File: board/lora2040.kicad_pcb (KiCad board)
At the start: 2 copper layers, 19 parts, among them U1 RP2040, U2 MR20H40, U3 RFM9xBreakout, Y1 ABM8-272-T3

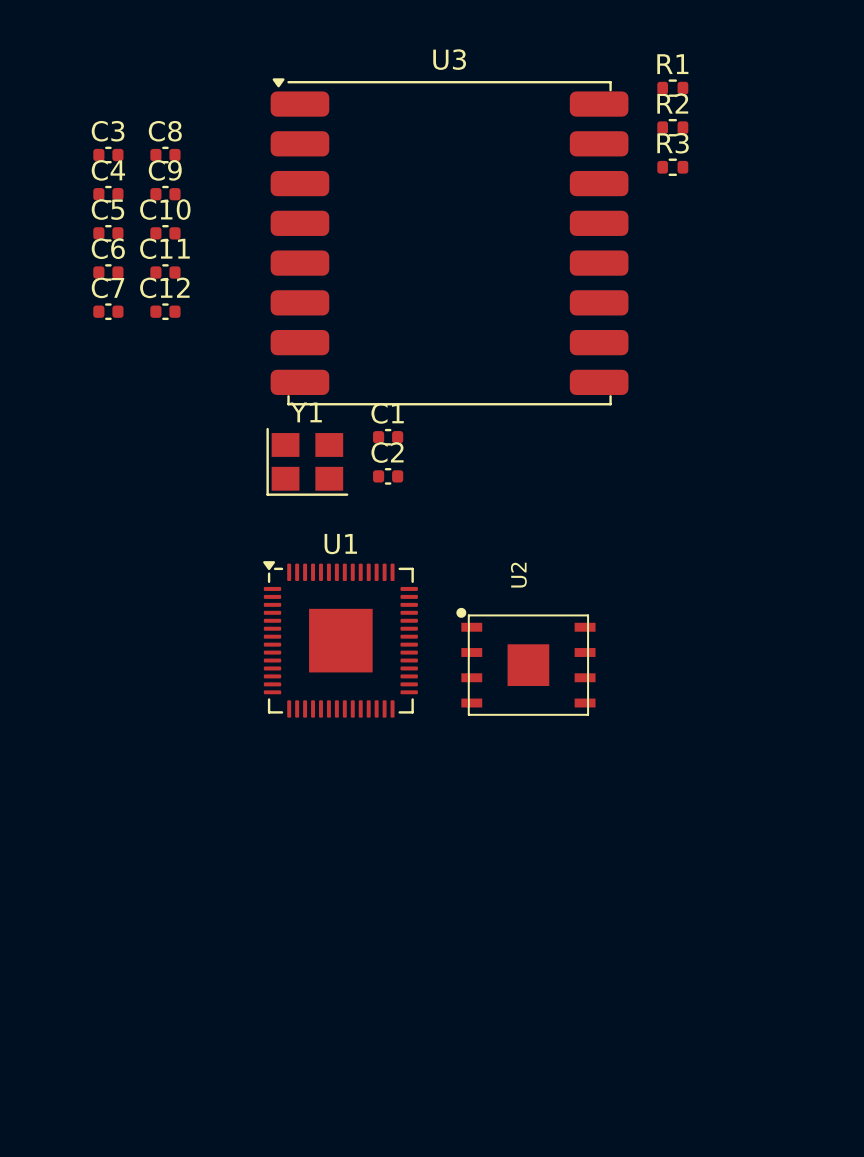
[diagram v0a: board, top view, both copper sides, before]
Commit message: added in sx1262 ref design
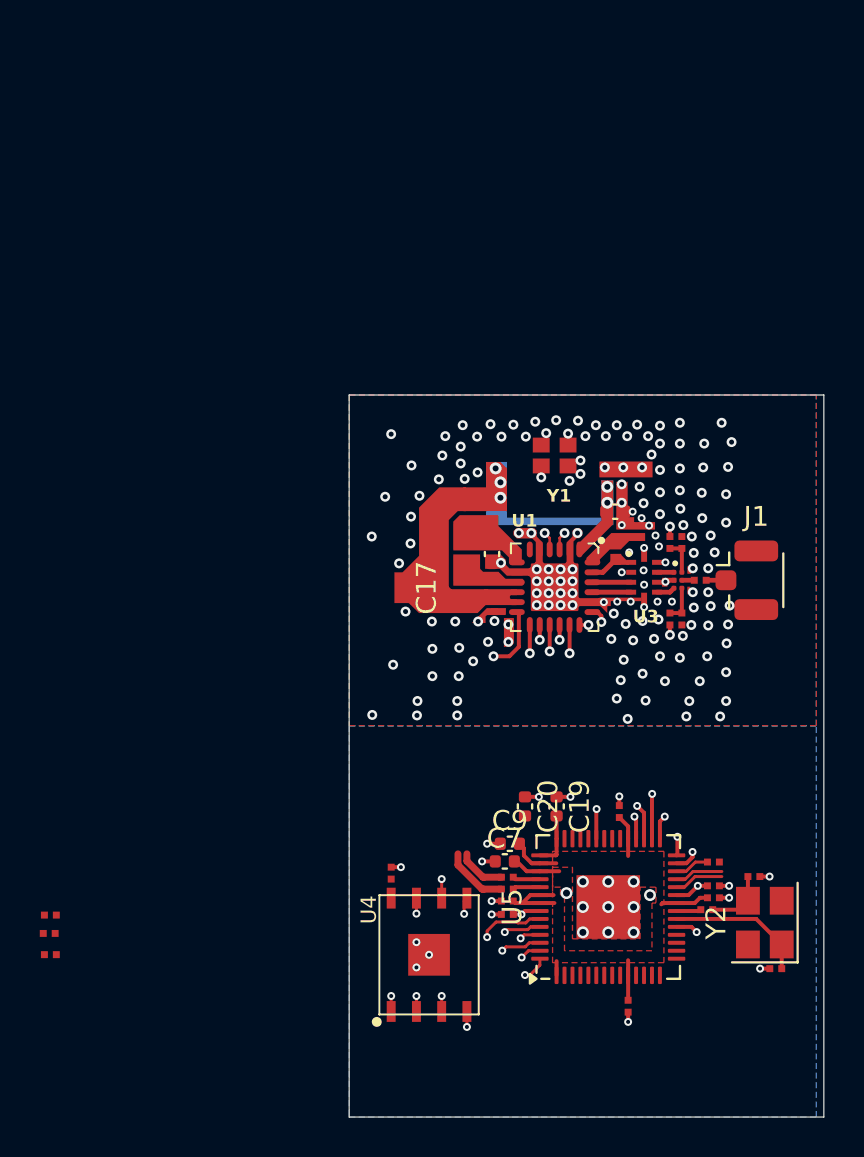
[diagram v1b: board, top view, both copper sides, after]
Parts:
- added C13: 0.1uF, custom-footprints:sx126x_C_0201, F.Cu at (151.0, 105.2)
- added C14: 1nF, custom-footprints:sx126x_C_0201, F.Cu at (149.4, 87.3)
- added C15: 1nF, custom-footprints:sx126x_C_0201, F.Cu at (149.4, 91.2)
- added C16: 0.1uF, Capacitor_SMD:C_0402_1005Metric, F.Cu at (146.1, 85.8)
- added C17: 470nF, Capacitor_SMD:C_0402_1005Metric, F.Cu at (139.9, 87.9)
- added C18: 0.1uF, custom-footprints:sx126x_C_0201, F.Cu at (140.0, 90.5)
- added C19: 0.1uF, Capacitor_SMD:C_0402_1005Metric, F.Cu at (143.1, 100.6)
- added C20: 0.1uF, Capacitor_SMD:C_0402_1005Metric, F.Cu at (141.6, 100.6)
- added C21: 0.1uF, custom-footprints:sx126x_C_0201, F.Cu at (134.8, 103.9)
- added J1: u.FL, Connector_Coaxial:U.FL_Hirose_U.FL-R-SMT-1_Vertical, F.Cu at (152.7, 89.2)
- added L1: 47nF, custom-footprints:sx126x_L_0402, F.Cu at (146.1, 87.8)
- added L7: 15uH, custom-footprints:sx126x_L_0805, F.Cu at (138.6, 87.8)
- added R4: 100, custom-footprints:sx126x_R_0201, F.Cu at (148.8, 87.3)
- added R5: 0, custom-footprints:sx126x_R_0201, F.Cu at (117.7, 108.0)
- added R6: 27, custom-footprints:sx126x_R_0201, F.Cu at (140.7, 104.7)
- added R7: 27, custom-footprints:sx126x_R_0201, F.Cu at (140.7, 104.1)
- added R8: 1K, custom-footprints:sx126x_R_0201, F.Cu at (150.7, 105.8)
- added R9: 10K, custom-footprints:sx126x_R_0201, F.Cu at (151.0, 103.4)
- added U4: MR20H40 or AS3004204, custom-footprints:SON127P600X500X90-9N, F.Cu at (136.7, 108.0)
- added U5: RP2040, Package_DFN_QFN:QFN-56-1EP_7x7mm_P0.4mm_EP3.2x3.2mm, F.Cu at (145.7, 105.6)
- added Y2: ABM8-272-T3, Crystal:Crystal_SMD_3225-4Pin_3.2x2.5mm, F.Cu at (153.6, 106.4)
- C1: value 15pF -> 47nF; footprint Capacitor_SMD:C_0402_1005Metric -> custom-footprints:sx126x_C_0201
- C10, C11, C12, C5: footprint Capacitor_SMD:C_0402_1005Metric -> custom-footprints:sx126x_C_0201
- C2: value 15pF -> 47pF; footprint Capacitor_SMD:C_0402_1005Metric -> custom-footprints:sx126x_C_0201
- C3: value 1uF -> 15pF; footprint Capacitor_SMD:C_0402_1005Metric -> custom-footprints:sx126x_C_0201
- C4: value 0.1uF -> 15pF; footprint Capacitor_SMD:C_0402_1005Metric -> custom-footprints:sx126x_C_0201
- C6: value 1uF -> 0.1uF; footprint Capacitor_SMD:C_0402_1005Metric -> custom-footprints:sx126x_C_0201
- C7, C9: value 0.1uF -> 1uF
- C8: value 0.1uF -> 39pF; footprint Capacitor_SMD:C_0402_1005Metric -> custom-footprints:sx126x_C_0201
- R1: value 27 -> 10K; footprint Resistor_SMD:R_0402_1005Metric -> custom-footprints:sx126x_R_0201
- R2: footprint Resistor_SMD:R_0402_1005Metric -> custom-footprints:sx126x_R_0201
- R3: value 27 -> 100; footprint Resistor_SMD:R_0402_1005Metric -> custom-footprints:sx126x_R_0201
- U1: value RP2040 -> SX1262IMLTRT; footprint Package_DFN_QFN:QFN-56-1EP_7x7mm_P0.4mm_EP3.2x3.2mm -> custom-footprints:VQFN24_4X4MM_SX126x
- U2: value MR20H40 -> BGS12WN6E6327; footprint custom-footprints:SON127P600X500X90-9N -> Package_LGA:Infineon_PG-TSNP-6-10_0.7x1.1mm_0.7x1.1mm_P0.4mm
- U3: value RFM9xBreakout -> 0900FM15K0039; footprint RF_Module:HOPERF_RFM9XW_SMD -> custom-footprints:0900FM15K0039
- Y1: value ABM8-272-T3 -> EXS00A-CS06465; footprint Crystal:Crystal_SMD_3225-4Pin_3.2x2.5mm -> custom-footprints:sx126x_Xtal
- moved C3 52.9 mm to (154.2, 108.7)
- moved R1 52.8 mm to (117.6, 107.0)
- moved R2 50.5 mm to (117.7, 106.0)
- moved C4 47.3 mm to (153.1, 104.1), turned to 180 degrees
- moved C10 45.3 mm to (146.7, 110.6), turned to 90 degrees
- moved C5 44.8 mm to (151.0, 104.6), turned to 180 degrees
- moved C6 38.0 mm to (140.7, 106.0)
- moved C9 37.0 mm to (140.8, 102.5)
- moved C11 36.0 mm to (140.7, 105.3)
- moved C8 34.4 mm to (150.4, 89.2), turned to 180 degrees
- moved C7 34.1 mm to (140.5, 103.3)
- moved C12 34.0 mm to (146.3, 100.8), turned to -90 degrees
- moved R3 22.7 mm to (148.8, 91.2), turned to -90 degrees
- moved U3 19.4 mm to (147.5, 89.1), turned to -90 degrees
- moved C2 13.1 mm to (147.4, 86.8), turned to -90 degrees
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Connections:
- C1 pad 2: /XIN -> Net-(U1-VR_PA)
- C10 pad 1: Net-(C10-Pad1) -> GND
- C11 pad 1: Net-(C10-Pad1) -> GND
- C12 pad 1: Net-(C10-Pad1) -> GND
- C2 pad 2: Net-(C2-Pad2) -> Net-(U1-VR_PA)
- C3 pad 2: +1V1 -> /XIN
- C4 pad 2: +1V1 -> Net-(C4-Pad2)
- C6 pad 2: +3V3 -> +1V1
- C7 pad 1: Net-(C10-Pad1) -> GND
- C7 pad 2: +3V3 -> +1V1
- C8 pad 1: Net-(C10-Pad1) -> Net-(J1-In)
- C8 pad 2: +3V3 -> Net-(U2-RFIN)
- C9 pad 1: Net-(C10-Pad1) -> GND
- R1 pad 1: /USB_D+ -> /QSPI_SS
- R1 pad 2: Net-(U1-USB_DP) -> +3V3
- R2 pad 1: Net-(C2-Pad2) -> Net-(R2-Pad1)
- R2 pad 2: /XOUT -> /QSPI_SS
- R3 pad 1: /USB_D- -> Net-(U2-VDD)
- R3 pad 2: Net-(U1-USB_DM) -> /ANT_SW
- U1 pad 1: +3V3 -> /VDD_RF
- U1 pad 10: +3V3 -> /VDD_RF
- U1 pad 11: unconnected-(U1-GPIO8-Pad11) -> /VDD_RF
- U1 pad 12: unconnected-(U1-GPIO9-Pad12) -> /RF_DIO2
- U1 pad 13: unconnected-(U1-GPIO10-Pad13) -> /RF_DIO1
- U1 pad 14: unconnected-(U1-GPIO11-Pad14) -> /RF_BUSY
- U1 pad 15: unconnected-(U1-GPIO12-Pad15) -> /RF_RST
- U1 pad 16: unconnected-(U1-GPIO13-Pad16) -> /SPI0_MISO_RX
- U1 pad 17: unconnected-(U1-GPIO14-Pad17) -> /SPI0_MOSI_TX
- U1 pad 18: unconnected-(U1-GPIO15-Pad18) -> /SPI0_SCK
- U1 pad 19: GND -> /SPI0_CS
- U1 pad 2: unconnected-(U1-GPIO0-Pad2) -> GND
- U1 pad 20: /XIN -> GND
- U1 pad 21: /XOUT -> Net-(U1-RFI_P)
- U1 pad 22: +3V3 -> Net-(U1-RFI_N)
- U1 pad 23: +1V1 -> Net-(U1-RFO)
- U1 pad 24: unconnected-(U1-SWCLK-Pad24) -> Net-(U1-VR_PA)
- U1 pad 25: unconnected-(U1-SWD-Pad25) -> GND
- U1 pad 3: unconnected-(U1-GPIO1-Pad3) -> Net-(U1-XTA)
- U1 pad 4: unconnected-(U1-GPIO2-Pad4) -> Net-(U1-XTB)
- U1 pad 5: unconnected-(U1-GPIO3-Pad5) -> GND
- U1 pad 6: unconnected-(U1-GPIO4-Pad6) -> /RF_DIO3
- U1 pad 7: unconnected-(U1-GPIO5-Pad7) -> Net-(U1-VREG)
- U1 pad 8: unconnected-(U1-GPIO6-Pad8) -> GND
- U1 pad 9: unconnected-(U1-GPIO7-Pad9) -> Net-(U1-DCC_SW)
- U2 pad 1: unconnected-(U2-~{CS}-Pad1) -> Net-(U2-RF2)
- U2 pad 2: Net-(U1-QSPI_SD1) -> GND
- U2 pad 3: unconnected-(U2-~{WP}-Pad3) -> Net-(U2-RF1)
- U2 pad 4: GND -> Net-(U2-VDD)
- U2 pad 5: Net-(U1-QSPI_SD0) -> Net-(U2-RFIN)
- U2 pad 6: Net-(U1-QSPI_SCLK) -> Net-(U2-CTRL)
- U3 pad 1: GND -> Net-(U1-RFO)
- U3 pad 2: unconnected-(U3-MISO-Pad2) -> GND
- U3 pad 3: unconnected-(U3-MOSI-Pad3) -> Net-(U1-RFI_N)
- U3 pad 4: unconnected-(U3-SCK-Pad4) -> Net-(U1-RFI_P)
- U3 pad 5: unconnected-(U3-CS-Pad5) -> GND
- U3 pad 6: unconnected-(U3-~{RESET}-Pad6) -> Net-(U2-RF1)
- U3 pad 7: unconnected-(U3-NC-Pad7) -> GND
- U3 pad 8: GND -> Net-(U2-RF2)
- U3 pad 9: unconnected-(U3-ANT-Pad9) -> GND
- Y1 pad 1: GND -> Net-(U1-XTB)
- Y1 pad 2: /XIN -> GND
- Y1 pad 3: GND -> Net-(U1-XTA)
- Y1 pad 4: Net-(C2-Pad2) -> GND
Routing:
- net /RF_DIO2: track 0.00 -> 37.7 mm, vias 0 -> 2
- net +3V3: track 0.00 -> 16.4 mm
- net /SPI0_MISO_RX: track 0.00 -> 15.9 mm, vias 0 -> 2
- net /SPI0_CS: track 0.00 -> 14.2 mm, vias 0 -> 2
- net /RF_BUSY: track 0.00 -> 13.2 mm, vias 0 -> 2
- net /RF_RST: track 0.00 -> 13.0 mm, vias 0 -> 2
- net /SPI0_SCK: track 0.00 -> 12.9 mm, vias 0 -> 2
- net /SPI0_MOSI_TX: track 0.00 -> 12.5 mm, vias 0 -> 2
- net /RF_DIO1: track 0.00 -> 12.1 mm, vias 0 -> 2
- net Net-(U4-SCK): track 0.00 -> 12.1 mm, vias 0 -> 2
- net /QSPI_SS: track 0.00 -> 9.82 mm, vias 0 -> 2
- net GND: track 0.00 -> 8.99 mm, vias 0 -> 187
- net Net-(U4-SO): track 0.00 -> 8.29 mm, vias 0 -> 2
- net /QSPI_SD3: track 0.00 -> 8.08 mm, vias 0 -> 2
- net /XIN: track 0.00 -> 7.10 mm
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- added copper zone on F.Cu, net +1V1
- added copper zone on F.Cu, net +3V3
- added copper zone on B.Cu, net GND
- added copper zone on F.Cu, net GND
- added copper zone on In1.Cu, net GND
- added copper zone on In2.Cu, net GND
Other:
- board outline added: 23.9 x 36.3 mm
- copper layers 2 -> 4

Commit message: about to switch to TXCO
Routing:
- net /SPI0_MISO_RX: track 15.9 -> 1.95 mm
- net /SPI0_CS: track 14.2 -> 1.78 mm
- net /RF_BUSY: track 13.2 -> 1.97 mm
- net /SPI0_SCK: track 12.9 -> 1.66 mm
- net /RF_RST: track 13.0 -> 3.12 mm
- net /RF_DIO1: track 12.1 -> 2.92 mm
- net /SPI0_MOSI_TX: track 12.5 -> 3.68 mm
- net /ANT_SW: track 6.41 -> 2.72 mm
- net unconnected-(U5-GPIO12-Pad15): track 0.00 -> 1.02 mm, vias 0 -> 1
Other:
- board text added: "Mitigate thermal effects on xtal"

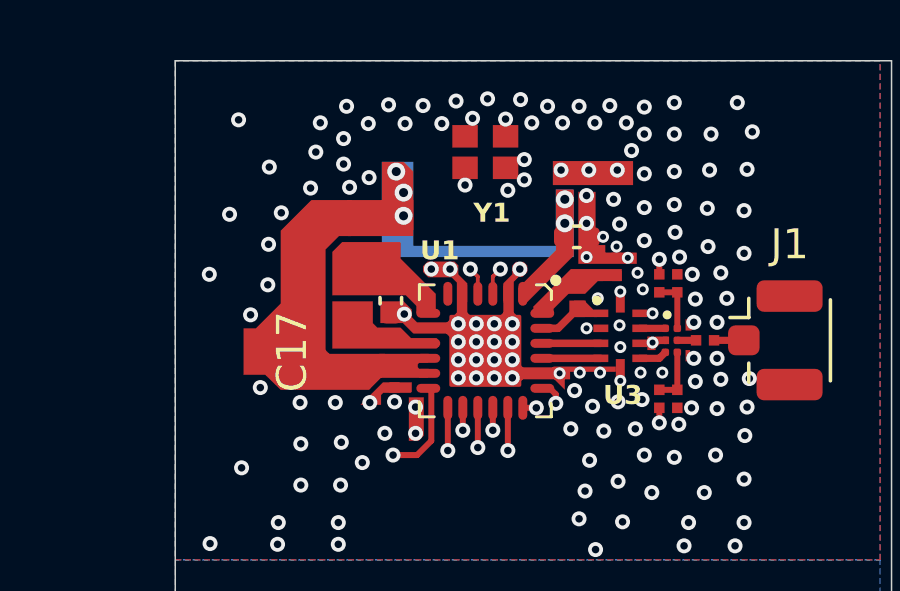
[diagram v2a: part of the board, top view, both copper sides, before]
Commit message: changed to TXCO
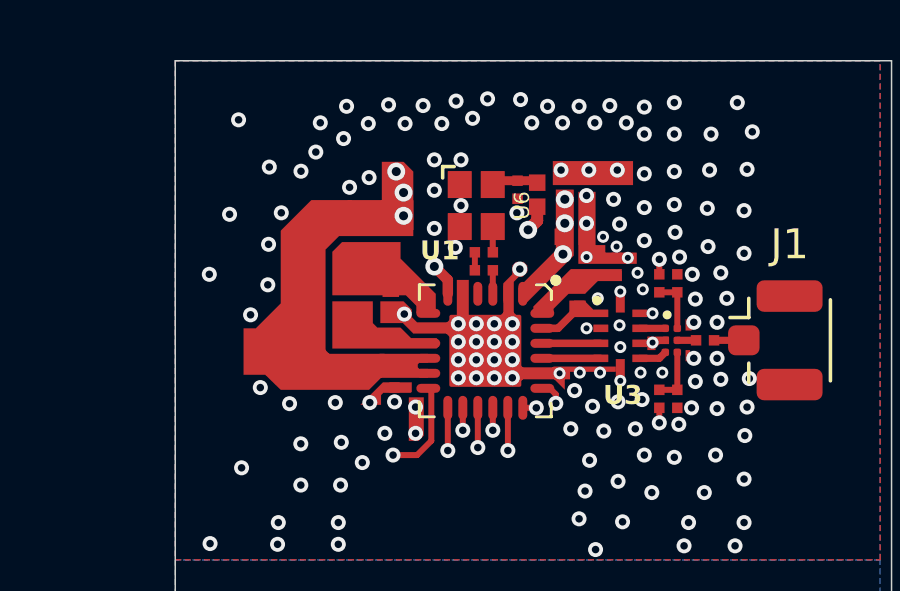
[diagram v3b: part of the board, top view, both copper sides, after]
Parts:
- removed Y1: EXS00A-CS06465, custom-footprints:sx126x_Xtal
- added C22: 10pF, custom-footprints:sx126x_C_0201, F.Cu at (143.0, 86.3)
- added C23: 0.1uF, custom-footprints:sx126x_C_0201, F.Cu at (144.1, 84.2)
- added FB1: BLM15PG100SN1D, custom-footprints:sx126x_L_0402, F.Cu at (144.8, 84.3)
- added R10: 220, custom-footprints:sx126x_R_0201, F.Cu at (143.0, 86.9)
- added U6: RTX-2016BD32-S-32.000-TR, custom-footprints:TXCO_2.0x1.6, F.Cu at (142.7, 84.7)
- C16: value 0.1uF -> 1uF; footprint Capacitor_SMD:C_0402_1005Metric -> custom-footprints:sx126x_C_0402
- C17: footprint Capacitor_SMD:C_0402_1005Metric -> custom-footprints:sx126x_C_0402
- moved C16 0.07 mm to (146.0, 85.8)
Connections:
- U1 pad 4: Net-(U1-XTB) -> unconnected-(U1-XTB-Pad4)
- U5 pad 15: unconnected-(U5-GPIO12-Pad15) -> /ANT_SW
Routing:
- net /RF_DIO2: track 37.7 -> 30.2 mm
- net Net-(U1-XTA): track 6.77 -> 0.78 mm, vias 2 -> 0
- net /RF_DIO3: track 0.00 -> 5.63 mm, vias 0 -> 2
- net Net-(U1-XTB): track 4.54 -> 0.00 mm, vias 2 -> 0
- net Net-(U6-VDD): track 0.00 -> 1.56 mm
- net unconnected-(U5-GPIO12-Pad15): track 1.02 -> 0.00 mm, vias 1 -> 0
- net /ANT_SW: track 2.72 -> 3.74 mm, vias 1 -> 2
- net Net-(U6-OUT): track 0.00 -> 0.86 mm
- net Net-(C22-Pad1): track 0.00 -> 0.60 mm
- net /VDD_RF: vias 5 -> 6
- added copper zone on In2.Cu, net /VDD_RF

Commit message: seeing what castelations look like
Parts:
- added C24: 1uF, Capacitor_SMD:C_0402_1005Metric, F.Cu at (136.8, 92.6)
- added C25: 10nF, Capacitor_SMD:C_0402_1005Metric, F.Cu at (140.1, 94.9)
- added C26: 1uF, Capacitor_SMD:C_0402_1005Metric, F.Cu at (135.6, 95.9)
- added J16: Conn_01x01, custom-footprints:castellated_07mm, F.Cu at (154.5, 84.7)
- added J16: Conn_01x01, custom-footprints:castellated_07mm, F.Cu at (133.3, 87.2)
- added J16: Conn_01x01, custom-footprints:castellated_07mm, F.Cu at (149.5, 111.3)
- added J16: Conn_01x01, custom-footprints:castellated_07mm, F.Cu at (154.5, 94.9)
- added J16: Conn_01x01, custom-footprints:castellated_07mm, F.Cu at (133.3, 89.8)
- added J16: Conn_01x01, custom-footprints:castellated_07mm, F.Cu at (146.9, 111.3)
- added J16: Conn_01x01, custom-footprints:castellated_07mm, F.Cu at (154.5, 107.3)
- added J16: Conn_01x01, custom-footprints:castellated_07mm, F.Cu at (133.3, 92.3)
- added J16: Conn_01x01, custom-footprints:castellated_07mm, F.Cu at (133.3, 109.9)
- added J16: Conn_01x01, custom-footprints:castellated_07mm, F.Cu at (154.5, 82.2)
- added J16: Conn_01x01, custom-footprints:castellated_07mm, F.Cu at (152.0, 111.3)
- added J16: Conn_01x01, custom-footprints:castellated_07mm, F.Cu at (133.3, 84.7)
- added J16: Conn_01x01, custom-footprints:castellated_07mm, F.Cu at (154.5, 109.9)
- added J16: Conn_01x01, custom-footprints:castellated_07mm, F.Cu at (144.4, 111.3)
- added J16: Conn_01x01, custom-footprints:castellated_07mm, F.Cu at (154.5, 97.4)
- added J16: Conn_01x01, custom-footprints:castellated_07mm, F.Cu at (133.3, 94.9)
- added J16: Conn_01x01, custom-footprints:castellated_07mm, F.Cu at (133.3, 82.2)
- added J16: Conn_01x01, custom-footprints:castellated_07mm, F.Cu at (133.3, 107.3)
- added J2: USB_B_Micro, Connector_USB:USB_Micro-B_Molex-105017-0001, F.Cu at (135.4, 101.6)
- added J3: Conn_01x04, Connector_JST:JST_SUR_BM04B-SURS-TF_1x04-1MP_P0.80mm_Vertical, F.Cu at (127.0, 102.4)
- added U7: TPS73633DBV, Package_TO_SOT_SMD:SOT-23-5, F.Cu at (137.9, 95.4)
- moved R2 25.9 mm to (143.3, 110.3), turned to -90 degrees
- moved R5 25.6 mm to (143.3, 109.0), turned to -90 degrees
- moved R1 22.1 mm to (139.7, 105.4), turned to 180 degrees
- moved C21 6.95 mm to (135.2, 110.9), turned to 0 degrees
- moved C19 3.92 mm to (141.8, 96.9)
- moved C11 3.78 mm to (139.8, 101.7)
- moved C3 3.78 mm to (153.3, 105.1)
- moved C4 3.78 mm to (152.2, 100.4)
- moved C5 3.78 mm to (150.2, 100.9)
- moved C6 3.78 mm to (139.8, 102.3)
- moved C7 3.78 mm to (139.7, 99.7)
- moved C9 3.78 mm to (140.0, 98.8)
- moved R7 3.78 mm to (139.8, 100.5)
- moved R8 3.78 mm to (149.9, 102.1)
- moved R9 3.78 mm to (150.2, 99.7)
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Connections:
- C16 pad 1: /VDD_RF -> +3V3
- C18 pad 1: /VDD_RF -> +3V3
- U1 pad 1: /VDD_RF -> +3V3
- U1 pad 10: /VDD_RF -> +3V3
- U1 pad 11: /VDD_RF -> +3V3
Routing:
- net Net-(U4-SCK): track 12.1 -> 2.86 mm
- net /QSPI_SS: track 9.82 -> 2.06 mm
- net +3V3: track 16.4 -> 23.8 mm, vias 0 -> 8
- net Net-(U4-SO): track 8.29 -> 1.84 mm
- net +1V1: track 5.62 -> 10.9 mm
- net Net-(U4-SI): track 5.49 -> 1.16 mm, vias 2 -> 1
- net /QSPI_SD3: track 8.08 -> 3.89 mm
- net /QSPI_SD2: track 6.83 -> 2.99 mm
- net unconnected-(U5-SWCLK-Pad24): track 2.50 -> 4.80 mm, vias 0 -> 1
- net /ANT_SW: track 3.74 -> 2.28 mm
- net unconnected-(U5-SWD-Pad25): track 2.44 -> 3.56 mm, vias 0 -> 1
- net GND: vias 187 -> 170
- net /VDD_RF: vias 6 -> 0
- added copper zone on In2.Cu, net +3V3
- removed copper zone on In2.Cu, net /VDD_RF
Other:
- board size 23.9 x 36.3 mm -> 22.4 x 31.1 mm

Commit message: routing tests
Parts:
- removed the J16 at (133.3, 109.9)
- removed the J16 at (154.5, 82.2)
- removed the J16 at (152.0, 111.3)
- removed the J16 at (154.5, 109.9)
- removed J3: Conn_01x04, Connector_JST:JST_SUR_BM04B-SURS-TF_1x04-1MP_P0.80mm_Vertical
- added C27: 10uF, Capacitor_SMD:C_0402_1005Metric, F.Cu at (136.2, 90.7)
- added J16: Conn_01x01, custom-footprints:castellated_07mm, F.Cu at (153.2, 82.7)
- added J16: Conn_01x01, custom-footprints:castellated_07mm, F.Cu at (153.2, 110.0)
- R2, R5: footprint custom-footprints:sx126x_R_0201 -> Resistor_SMD:R_0402_1005Metric
- moved J16 1.46 mm to (134.6, 82.7), turned to -45 degrees
- moved R2 1.13 mm to (143.5, 109.2)
- moved C21 0.86 mm to (135.0, 110.0), turned to -45 degrees
- moved R5 0.84 mm to (144.0, 108.7), turned to 180 degrees
- moved C24 0.83 mm to (137.5, 92.8)
- moved J16 0.51 mm to (133.4, 106.8)
- moved J16 0.48 mm to (154.5, 106.8)
- moved U4 0.28 mm to (139.4, 108.7)
- moved J16 0.17 mm to (133.4, 87.2)
- moved J16 0.17 mm to (133.4, 89.8)
- moved J16 0.17 mm to (133.4, 92.3)
- moved J16 0.17 mm to (133.4, 84.7)
- moved J16 0.17 mm to (133.4, 94.9)
- moved J2 0.17 mm to (135.6, 101.6)
- moved C19 0.15 mm to (141.9, 96.9)
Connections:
- net /ANT_SW renamed /RF_SW_PWR
- U5 pad 2: unconnected-(U5-GPIO0-Pad2) -> /UART0_TX
- U5 pad 3: unconnected-(U5-GPIO1-Pad3) -> /UART0_RX
- U5 pad 6: unconnected-(U5-GPIO4-Pad6) -> /I2C0_SDA
- U5 pad 7: unconnected-(U5-GPIO5-Pad7) -> /I2C0_SCL
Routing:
- net +3V3: track 23.8 -> 50.6 mm, vias 8 -> 17
- net /RF_SW_PWR: track 2.28 -> 15.6 mm
- net unconnected-(U5-GPIO27_ADC1-Pad39): track 0.00 -> 13.2 mm, vias 0 -> 1
- net unconnected-(U5-GPIO28_ADC2-Pad40): track 0.00 -> 11.6 mm, vias 0 -> 1
- net /SPI0_MISO_RX: track 1.94 -> 11.9 mm
- net Net-(U4-SCK): track 2.86 -> 12.1 mm
- net /SPI0_CS: track 1.78 -> 10.4 mm
- net /QSPI_SS: track 2.06 -> 10.7 mm
- net /RF_BUSY: track 1.97 -> 9.21 mm
- net /QSPI_SD3: track 3.89 -> 11.1 mm
- net /SPI0_SCK: track 1.96 -> 8.62 mm
- net Net-(U4-SI): track 1.16 -> 7.11 mm, vias 1 -> 2
- net Net-(U4-SO): track 1.84 -> 7.64 mm
- net /VUSB: track 0.00 -> 5.62 mm, vias 0 -> 2
- net /I2C0_SCL: track 0.00 -> 5.48 mm, vias 0 -> 1
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- removed copper zone on In2.Cu, net GND
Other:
- outline, holes or cut-outs redrawn
- board text added: "HOLLIDAY"
